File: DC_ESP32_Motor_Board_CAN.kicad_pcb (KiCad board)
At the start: 2 copper layers, 29.8 x 46.2 mm, 44 parts, among them IC1 VNH7100BASTR, IC2 TJA1050T_CM, IC3 LSM6DS3TR-C, J1 SM04B-SRSS-TB, J2 SM04B-SRSS-TB, J3 XT30PB, J4 XT30PB, J5 SM04B-SRSS-TB, J6 SM04B-SRSS-TB, J7 XT30PB, J8 Conn_01x03_Pin, Q1 BSS138, Q2 BSS138, SW1 DSHP04TJGER, U1 MOUDLE-SEEEDUINO-XIAO-ESP32C3

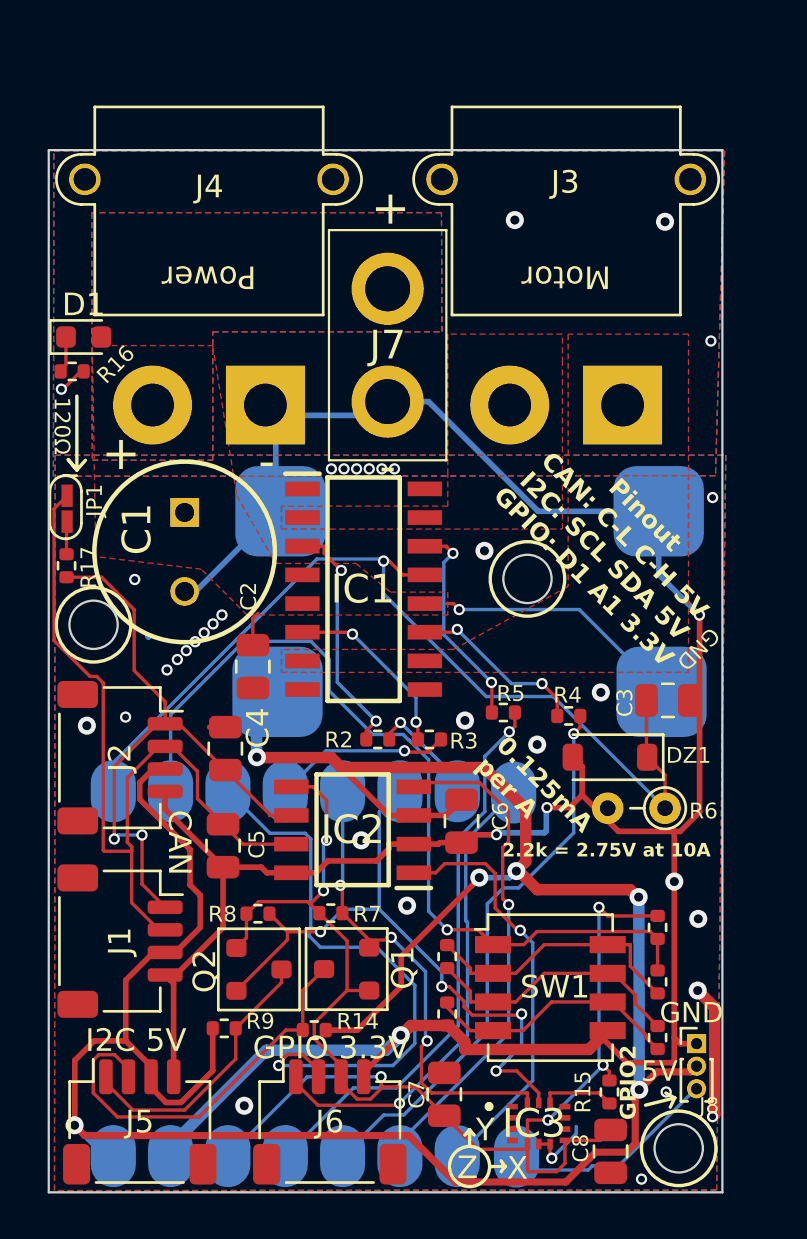
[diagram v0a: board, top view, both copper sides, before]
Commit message: Updates for PCB
Bigger GPIO2
Added RGB LED
Updated xt30s
Updated xt30 size to fit inline connectors on PCB
Fixed jst sh connections
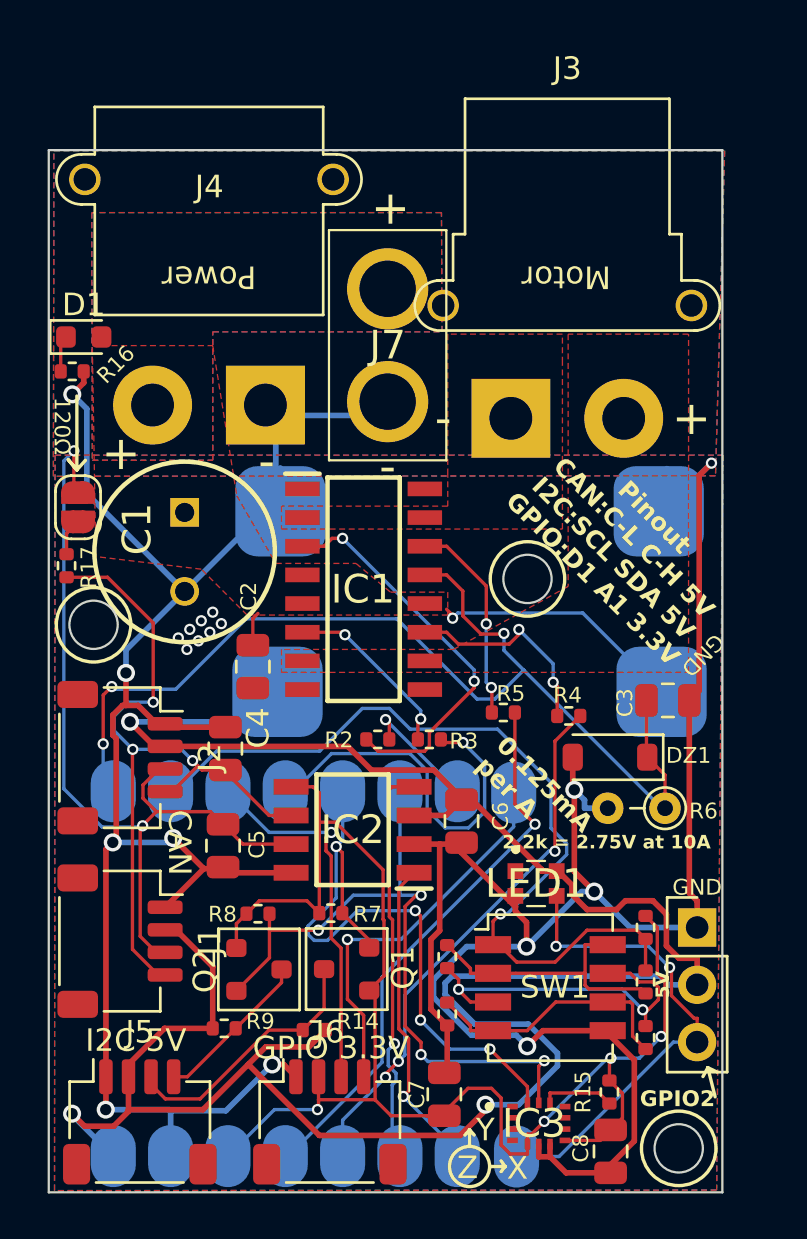
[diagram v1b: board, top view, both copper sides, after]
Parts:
- added LED1: WS2812C-2020, SamacSys_Parts:WS2812C2020, F.Cu at (98.9, 86.8)
- J3: footprint Library:Xt30 Horizontal -> JST_Sorted:xt30_90_Female
- J8: footprint Connector_PinHeader_1.00mm:PinHeader_1x03_P1.00mm_Vertical -> Connector_PinHeader_2.54mm:PinHeader_1x03_P2.54mm_Vertical
- R1: value 8.2k -> 22k
- R10: value 3.9k -> 10k
- R11: value 2.2k -> 4.7k
- R12: value 1.1k -> 2.2k
- R13: value 8.2k -> 10k
- moved J8 5.15 mm to (106.0, 88.8)
- moved J3 4.99 mm to (97.8, 66.2)
- moved R1 0.53 mm to (103.8, 91.2)
- moved R11 0.53 mm to (103.8, 93.7)
- moved R13 0.53 mm to (103.8, 88.8)
- moved JP1 0.36 mm to (78.6, 70.2)
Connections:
- J1 pad 1: CANL -> GND
- J1 pad 2: CANH -> +5V
- J1 pad 3: +5V -> CANH
- J1 pad 4: GND -> CANL
- J2 pad 1: CANL -> GND
- J2 pad 2: CANH -> +5V
- J2 pad 3: +5V -> CANH
- J2 pad 4: GND -> CANL
- J3 pad 1: /OUTB -> /OUTA
- J3 pad 2: /OUTA -> /OUTB
- J4 pad : GND -> (no net)
- J5 pad 1: /SCL5 -> GND
- J5 pad 2: /SDA5 -> +5V
- J5 pad 3: +5V -> /SDA5
- J5 pad 4: GND -> /SCL5
- J6 pad 1: GPIO_1 -> GND
- J6 pad 2: GPIO_A -> +3.3V
- J6 pad 3: +3.3V -> GPIO_A
- J6 pad 4: GND -> GPIO_1
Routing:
- net GND: track 138.2 -> 172.3 mm, vias 39 -> 19
- net +5V: track 116.9 -> 104.4 mm, vias 6 -> 3
- net GPIO_2: track 9.71 -> 21.7 mm, vias 0 -> 2
- net GPIO_A: track 26.1 -> 16.5 mm
- net INB: track 7.90 -> 16.7 mm
- net SDA: track 21.1 -> 29.1 mm, vias 3 -> 4
- net Net-(IC1-INA): track 10.8 -> 17.5 mm
- net /SDA5: track 18.1 -> 11.7 mm
- net RSENSE: track 42.1 -> 47.7 mm, vias 1 -> 3
- net CANL: track 27.7 -> 33.0 mm, vias 2 -> 3
- net /SCL5: track 12.3 -> 7.09 mm
- net CANTX: track 18.6 -> 14.1 mm
- net CANRX: track 22.3 -> 18.0 mm
- net Net-(R10-Pad1): track 11.9 -> 16.1 mm, vias 0 -> 2
- net GPIO_1: track 21.2 -> 17.3 mm
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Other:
- board text added: "Pinout CAN:C-L C-H 5V I2C:SCL SDA 5V GPIO:D1 A1 3.3V"
- board text removed: "Pinout CAN: C-L C-H 5V I2C: SCL SDA 5V GPIO: D1 A1 3.3V"

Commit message: Newest Update for Review
Updated do not place parts, and fixed last last few traces. Should be good for ordering
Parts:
- added D2: SS34, Diode_SMD:D_SOD-123, F.Cu at (88.6, 80.3)
- added JP2: SolderJumper_2_Open, CutomParts:Jumper Connected 2 Pin Small, F.Cu at (78.1, 60.2)
- moved R2 0.59 mm to (92.2, 81.0)
- moved R3 0.52 mm to (94.2, 81.0)
- moved JP1 0.13 mm to (78.5, 70.2)
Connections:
- R16 pad 2: Net-(D1-K) -> Net-(JP2-A)
- VR1 pad 3: +24V -> Net-(D2-K)
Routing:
- net Net-(D2-K): track 0.00 -> 19.1 mm, vias 0 -> 1
- net GND: track 172.3 -> 154.5 mm, vias 19 -> 6
- net +5V: track 104.4 -> 86.8 mm, vias 3 -> 5
- net INB: track 16.7 -> 8.79 mm
- net RSENSE: track 47.7 -> 40.2 mm, vias 3 -> 1
- net Net-(JP2-A): track 0.00 -> 6.18 mm
- net SCL: track 31.3 -> 26.3 mm, vias 4 -> 2
- net SDA: track 29.1 -> 24.4 mm, vias 4 -> 2
- net +3.3V: track 66.2 -> 62.5 mm, vias 4 -> 3
- net SEL: track 24.7 -> 28.3 mm
- net Net-(R10-Pad1): track 16.1 -> 12.7 mm, vias 2 -> 0
- net CANL: track 33.0 -> 29.9 mm, vias 3 -> 0
- net PWM: track 24.0 -> 26.4 mm, vias 3 -> 1
- net Net-(R11-Pad1): track 11.7 -> 13.9 mm
- net Net-(IC1-INA): track 17.5 -> 15.5 mm
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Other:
- board text added: "1/14/25 Rev 3 DAISY BOARD DC By Lucas Wilson & Will Thayer"
- board text added: "LED"
- board text removed: "10/27/24 DAISY BOARD DC By Lucas Wilson & Will Thayer"
